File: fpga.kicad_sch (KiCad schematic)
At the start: 63 parts, among them CON1 SD_Card_DM3BT, P10 CONN_01X01, P11 CONN_01X01, P12 CONN_01X01, P13 CONN_01X01, P14 CONN_01X01, P15 CONN_01X01, P16 CONN_01X01, P3 CONN_02X04, P4 CONN_02X04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

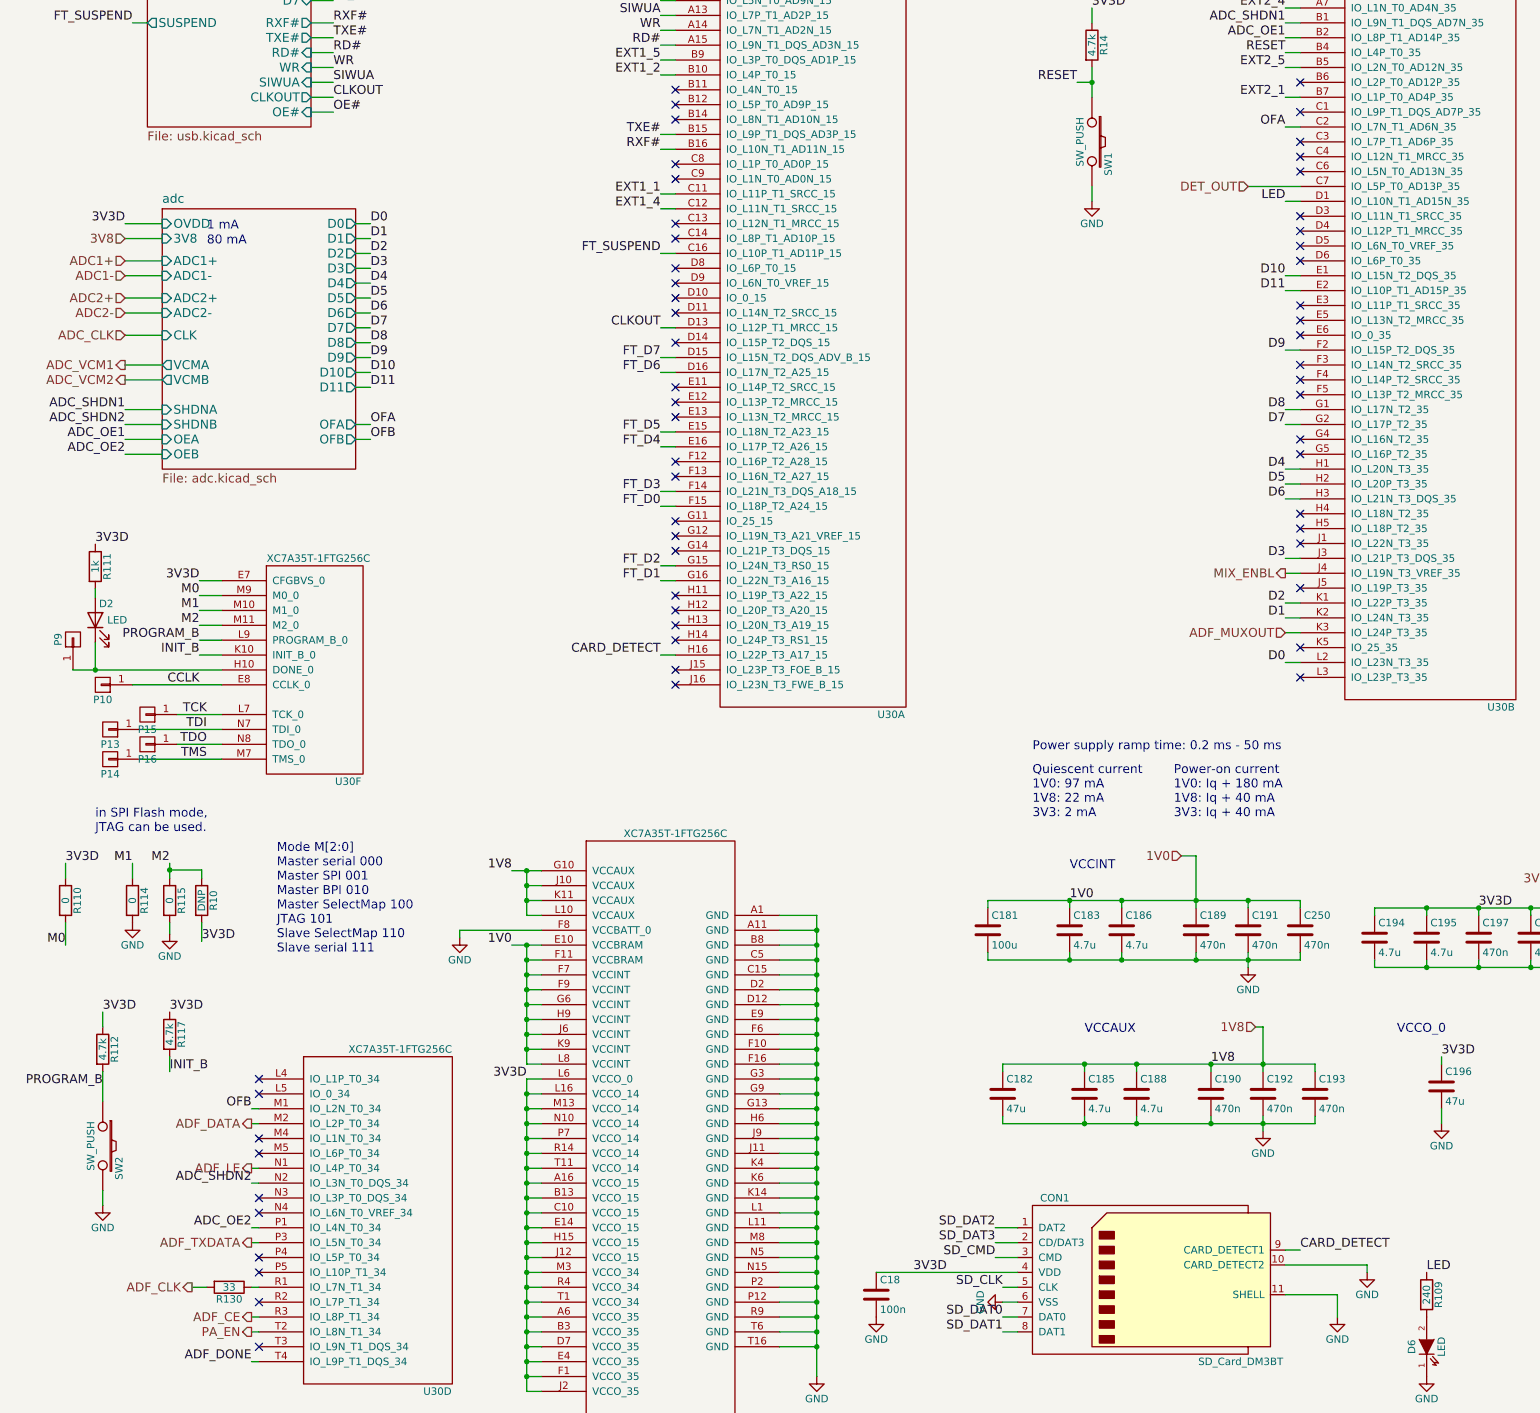
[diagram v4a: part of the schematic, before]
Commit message: clock buffer and txco source is changed. Clock is clipped sin and fanout says cmos square out but it is better anyways. Also traces are 50 ohm as well. Copper pours other minor thinks are changed as well
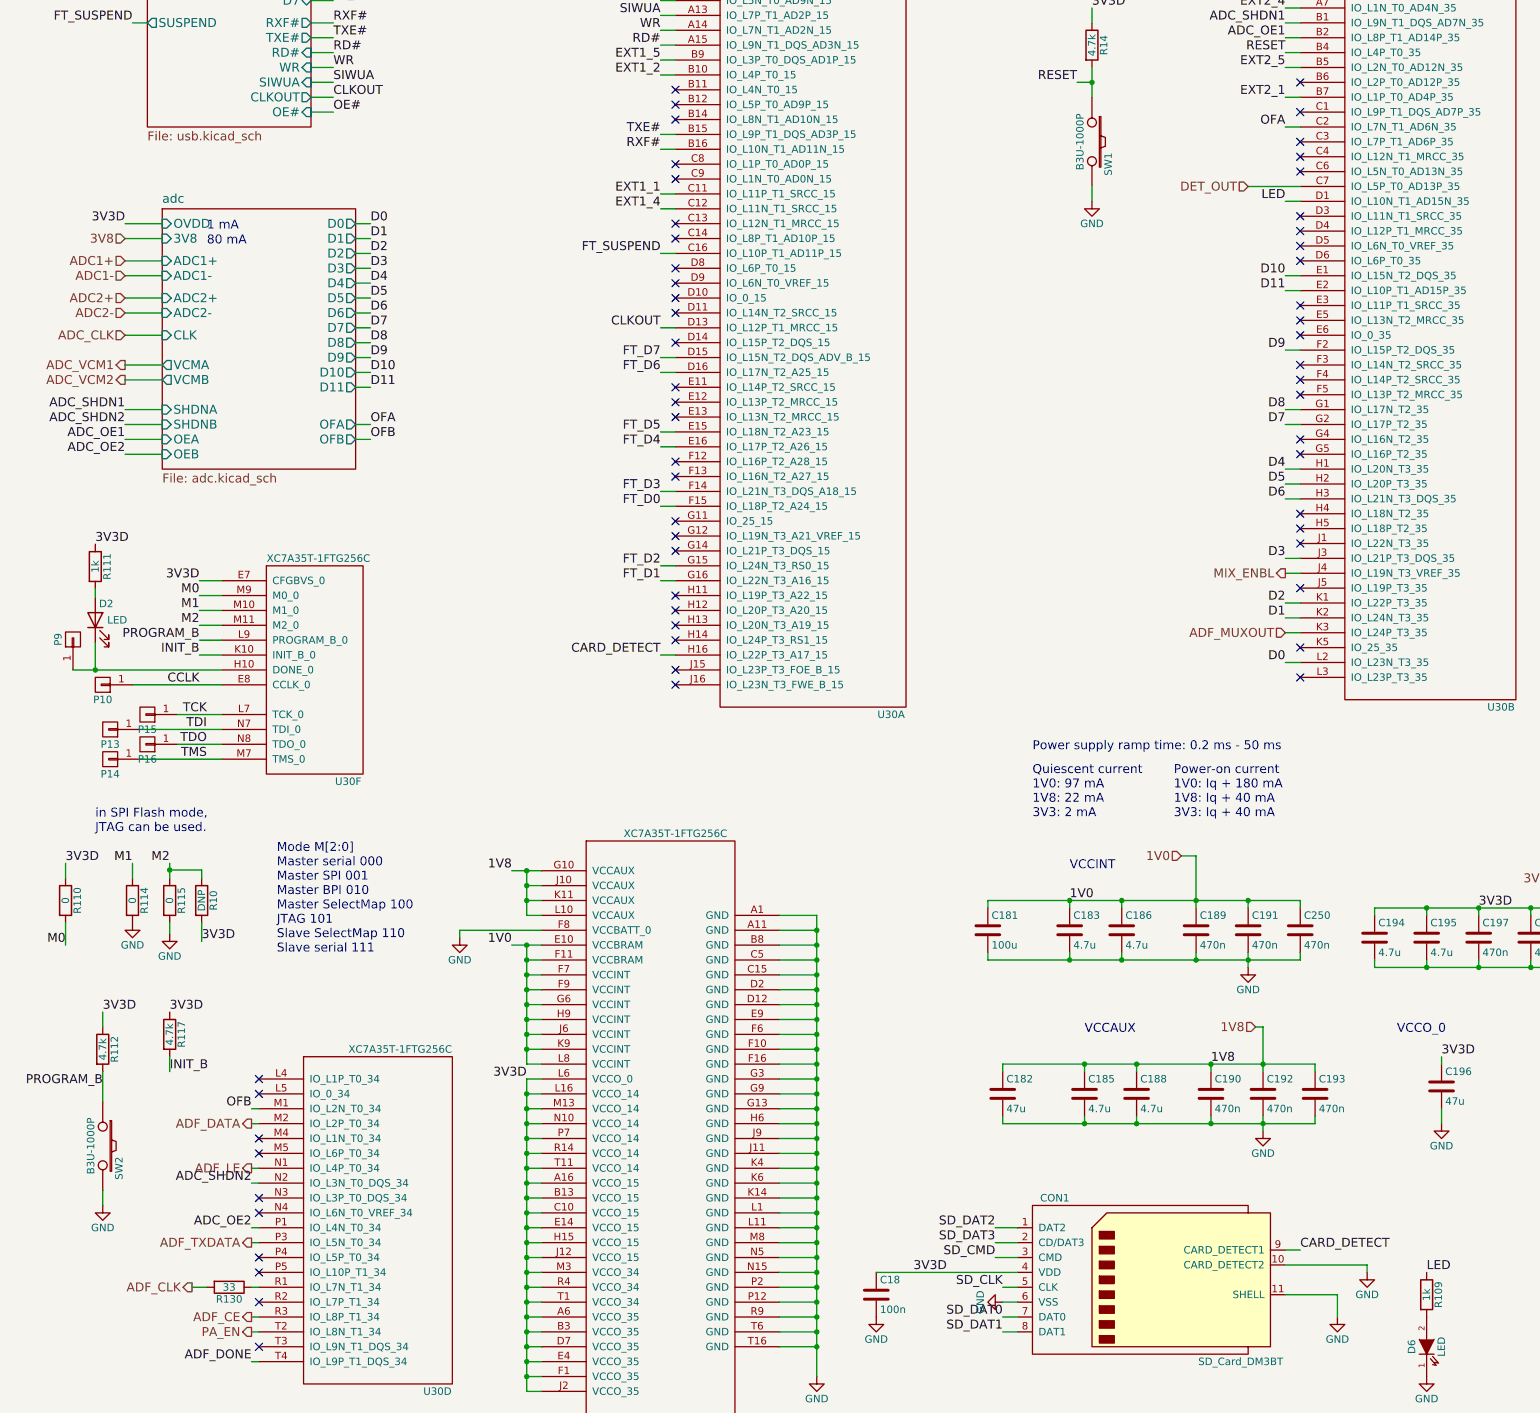
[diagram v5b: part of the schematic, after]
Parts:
- R109: value 240 -> 1k
- SW1, SW2: value SW_PUSH -> B3U-1000P
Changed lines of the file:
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@@
 			)
 		)
-		(property "Value" "240"
+		(property "Value" "1k"
 			(at 251.46 257.81 90)
 			(effects
@@
 			)
 		)
-		(property "Value" "SW_PUSH"
+		(property "Value" "B3U-1000P"
 			(at 23.368 232.41 0)
 			(effects
@@
 			)
 		)
-		(property "Value" "SW_PUSH"
+		(property "Value" "B3U-1000P"
 			(at 192.278 60.96 0)
 			(effects

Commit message: hardware changes
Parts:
- removed C170, C171, C187, C189, C190, C191, C192, C193, C197, C198, C199, C200, C201, C202, C203, C204, C250, C251: 470n, Footprints:SMD_0402, symbol fmcw3-rescue:C
- removed C174: DNP, Footprints:SMD_0402, symbol fmcw3-rescue:C
- removed C18, C252: 100n, Footprints:SMD_0402, symbol fmcw3-rescue:C
- removed C181: 100u, Footprints:SMD_1210, symbol fmcw3-rescue:C
- removed C182, C184, C196: 47u, Footprints:SMD_1206, symbol fmcw3-rescue:C
- removed C183, C185, C186, C188, C194, C195: 4.7u, Footprints:SMD_0603, symbol fmcw3-rescue:C
- removed CON1: SD_Card_DM3BT, fmcw3:DM3BT-DSF-PEJS, symbol fmcw3:SD_Card_DM3BT
- removed D6: LED, Footprints:Diode_0603, symbol fmcw3-rescue:LED
- removed P3, P4: CONN_02X04, Pin_Headers:Pin_Header_Straight_2x04_Pitch2.54mm_SMD, symbol fmcw3-rescue:CONN_02X04
- removed P9: CONN_01X01, fmcw3:TP_1.00, symbol fmcw3-rescue:CONN_01X01
- removed Q2: DNP(RE1C002UN), fmcw3:SOT-416, symbol fmcw3:MOS_N_GSD
- removed R10: DNP, Footprints:SMD_0402, symbol fmcw3-rescue:R
- removed R109: 1k, Footprints:SMD_0402, symbol fmcw3-rescue:R
- removed R110, R114, R115: 0, Footprints:SMD_0402, symbol fmcw3-rescue:R
- removed R112, R117, R118, R14: 4.7k, Footprints:SMD_0402, symbol fmcw3-rescue:R
- removed SW1, SW2: B3U-1000P, fmcw3:EVP-AWBA2A, symbol fmcw3-rescue:SW_PUSH
- removed U40: W25Q32JV, Housings_DFN_QFN:DFN-S-8-1EP_6x5mm_Pitch1.27mm, symbol fmcw3:W25Q32JV
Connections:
- net ADF_DONE: no longer names the net of U30.T4 (IO_L9P_T1_DQS_34)
- net CCLK renamed SPI_CLK
- net CLK_REF renamed FPGA_CLK
- net EXT1_1 renamed PIN1
- net EXT1_2 renamed PIN2
- net EXT1_3 renamed PIN3
- net EXT1_4 renamed PIN4
- net EXT1_5 renamed PIN5
- net EXT1_6 renamed PIN6
- net EXT2_1 renamed PIN7
- net EXT2_2 renamed PIN8
- net EXT2_3 renamed PIN9
- net EXT2_4 renamed PIN10
- net EXT2_5 renamed PIN11
- net EXT2_6 renamed PIN12
- net LED renamed USER_LED
- net PROGRAM_B renamed PROG_B
- net SPI_DIN renamed SPI_MISO
- no-connect marks 101 -> 102
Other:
- added sheet fpga_config (fpga_config.kicad_sch)
- note removed: "1 mA"
- note removed: "70 mA"
- note removed: "80 mA"
- note removed: "Mode M[2:0] Master serial 000 Master SPI 001 Master BPI 010 Master SelectMap 100 JTAG 101 Slave SelectMap 110 Slave serial 111"
- note removed: "Power supply ramp time: 0.2 ms - 50 ms"
- note removed: "Power-on current 1V0: Iq + 180 mA 1V8: Iq + 40 mA 3V3: Iq + 40 mA"
- note removed: "Quiescent current 1V0: 97 mA 1V8: 22 mA 3V3: 2 mA"
- note removed: "VCCAUX"
- note removed: "VCCBRAM"
- note removed: "VCCINT"
- note removed: "VCCO"
- note removed: "VCCO_0"
- note removed: "in SPI Flash mode, JTAG can be used."
- moved on the sheet: C205, D2, P10, P11, P12, P13, P14, P15, P16, R111, R130, R69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

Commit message: hardware changes
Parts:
- removed P10, P11, P12, P13, P14, P15, P16: CONN_01X01, fmcw3:TP_1.00, symbol fmcw3-rescue:CONN_01X01
- added JP1, JP2, JP3, JP4: SolderJumper_2_Bridged, Footprints:SolderPad_2_Bridge, symbol Jumper:SolderJumper_2_Bridged
- added U35, U38, U4, U41, U42, U43, U44: SolderPad_1_Circle, Footprints:SolderPad_1_1.0mm_SMD_Circle, symbol SolderPad_1_Circle:SolderPad_1_Circle
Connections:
- net SPI_CLK: now also U42.1
- net SPI_MISO: now also U44.1
- net SPI_MOSI: now also U43.1
- net TCK: now also JP4.1 (A), U4.1
- net TDI: now also JP3.1 (A), U35.1
- net TDO: now also JP2.1 (A), U38.1
- net TMS: now also JP1.1 (A), U41.1
- net USER_LED: now also U30.B12 (IO_L5P_T0_AD9P_15); no longer U30.D1 (IO_L10N_T1_AD15N_35)
- new net FT_TCK: JP4.2 (B)
- new net FT_TDI: JP3.2 (B)
- new net FT_TDO: JP2.2 (B)
- new net FT_TMS: JP1.2 (B)

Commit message: schematic is updated pcb is almost done
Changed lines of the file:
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@@
 		)
 	)
-	(hierarchical_label "ADC_VCM2"
+	(hierarchical_label "ADC_VCMB"
 		(shape output)
 		(at 132.08 203.2 180)
@@
 		)
 	)
-	(hierarchical_label "ADC_VCM1"
+	(hierarchical_label "ADC_VCMA"
 		(shape output)
 		(at 132.08 200.66 180)
